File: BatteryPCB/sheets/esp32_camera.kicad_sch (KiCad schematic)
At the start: 10 parts, among them J1 ESP32 left, J2 ESP32 right, J3 RunCam Split 4

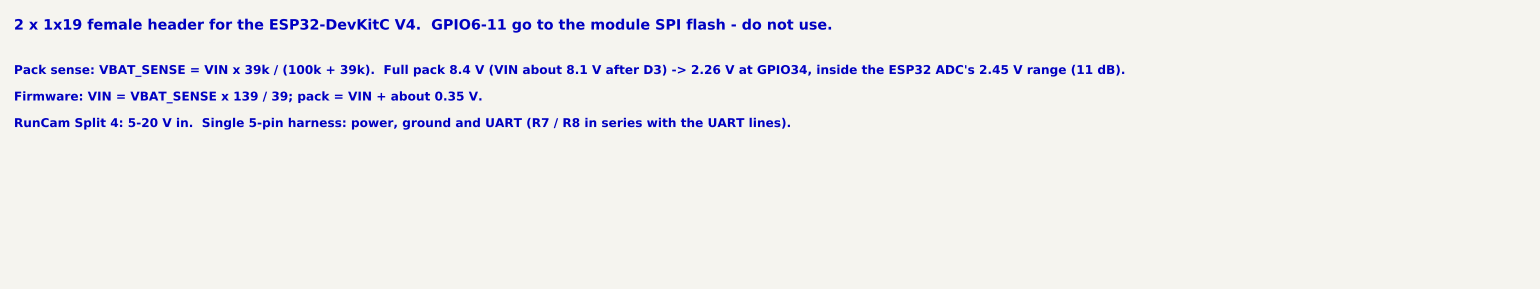
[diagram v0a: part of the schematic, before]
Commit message: Preserve battery PCB progress and prepare partial JLC assembly files
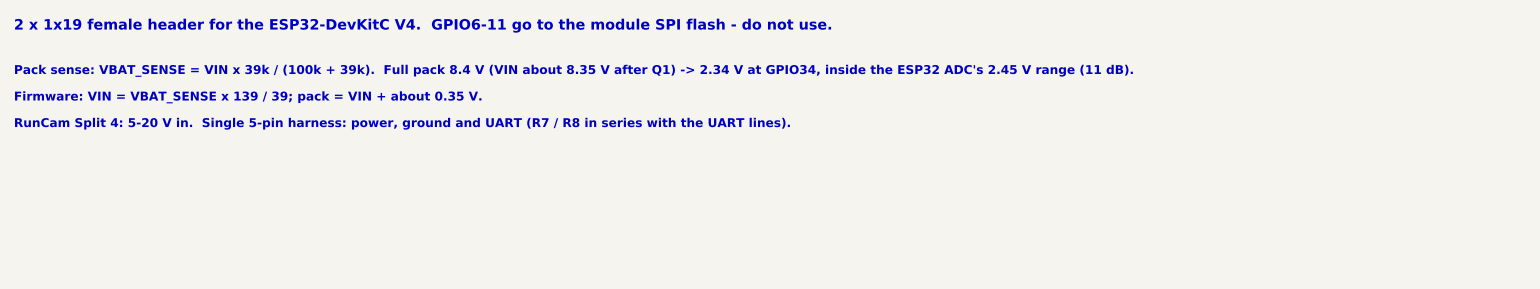
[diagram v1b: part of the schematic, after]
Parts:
- D2: LCSC (none) -> C84256; MPN LTST-C171KRKT -> NCD0805R1; Manufacturer Lite-On -> Foshan NationStar Optoelectronics
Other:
- note added: "Pack sense: VBAT_SENSE = VIN x 39k / (100k + 39k). Full pack 8.4 V (VIN about 8.35 V after Q1) -> 2.34 V at GPIO34, inside the ESP32 ADC's 2.45 V range (11 dB)."
- note removed: "Pack sense: VBAT_SENSE = VIN x 39k / (100k + 39k). Full pack 8.4 V (VIN about 8.1 V after D3) -> 2.26 V at GPIO34, inside the ESP32 ADC's 2.45 V range (11 dB)."
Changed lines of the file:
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@@
 		)
 	)
-	(text "Pack sense: VBAT_SENSE = VIN x 39k / (100k + 39k).  Full pack 8.4 V (VIN about 8.1 V after D3) -> 2.26 V at GPIO34, inside the ESP32 ADC's 2.45 V range (11 dB)."
+	(text "Pack sense: VBAT_SENSE = VIN x 39k / (100k + 39k).  Full pack 8.4 V (VIN about 8.35 V after Q1) -> 2.34 V at GPIO34, inside the ESP32 ADC's 2.45 V range (11 dB)."
 		(exclude_from_sim no)
 		(at 25.4 36.83 0)
@@
 		(pin "2"
 		)
-		(instances
+		    (property "Manufacturer" "Foshan NationStar Optoelectronics"
+      (at 0 0 0)
+      (effects (font (size 1.27 1.27)) (hide yes))
+    )
+        (property "MPN" "NCD0805R1"
+      (at 0 0 0)
+      (effects (font (size 1.27 1.27)) (hide yes))
+    )
+        (property "LCSC" "C84256"
+      (at 0 0 0)
+      (effects (font (size 1.27 1.27)) (hide yes))
+    )
+    (instances
 			(project "battery_pcb"
 				(path "/19ef3a32-de7c-46ee-a850-2420f6d47f94/51707861-a38d-47a0-88b0-b003633f2c22"
